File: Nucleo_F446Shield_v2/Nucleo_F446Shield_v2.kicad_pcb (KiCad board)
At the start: 2 copper layers, 48 parts, among them J1 Barrel_Jack, J11 CAN1, J12 CAN2, J15 CAN1, J16 CAN2, J19 I2C3, J20 UART4, J21 xt60 male, J3 CAN1, J4 CAN2, J7 CAN1, J8 CAN2, M3 TJA1050_Module, M4 TJA1050_Module, SW1 SW1, SW11 DIP1, SW2 SW2, SW3 SW3, U1 NUCLEO-F446RE, U2 MP1584

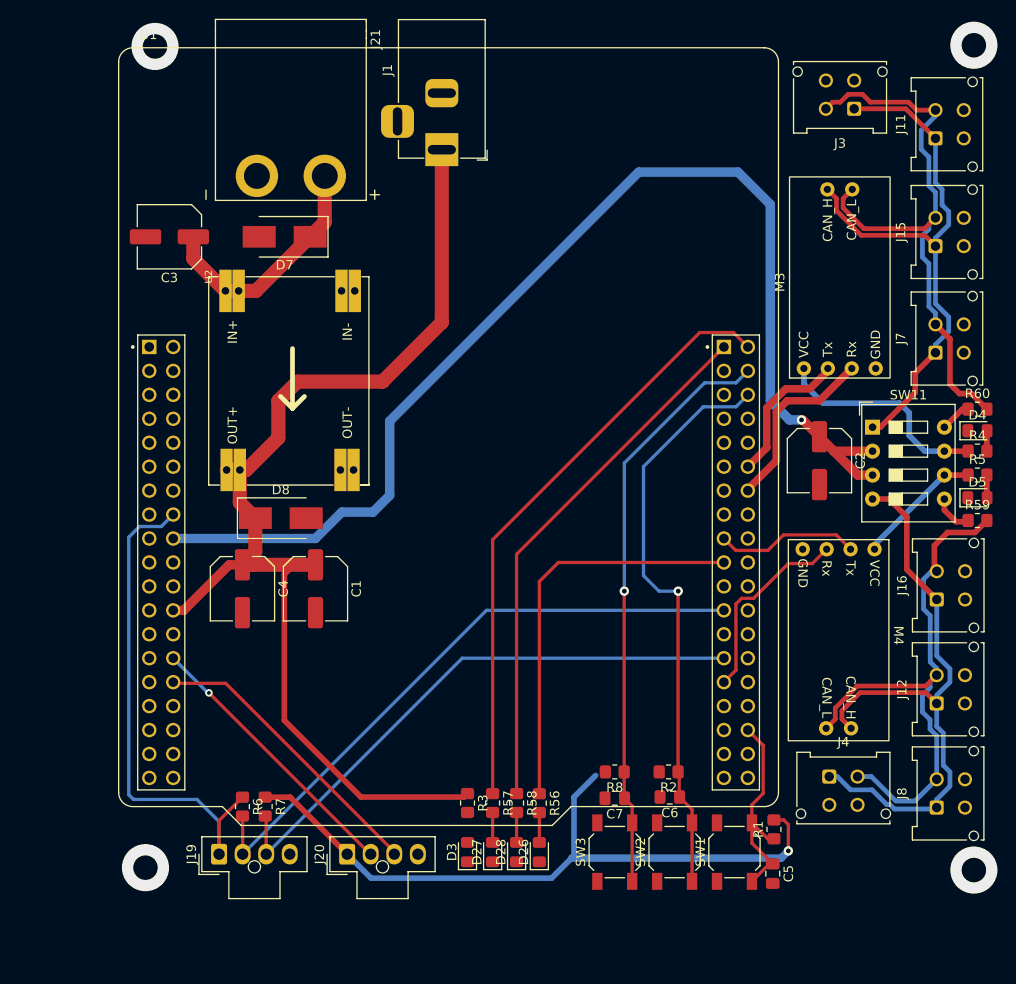
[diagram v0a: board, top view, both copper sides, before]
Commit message: add V2 board
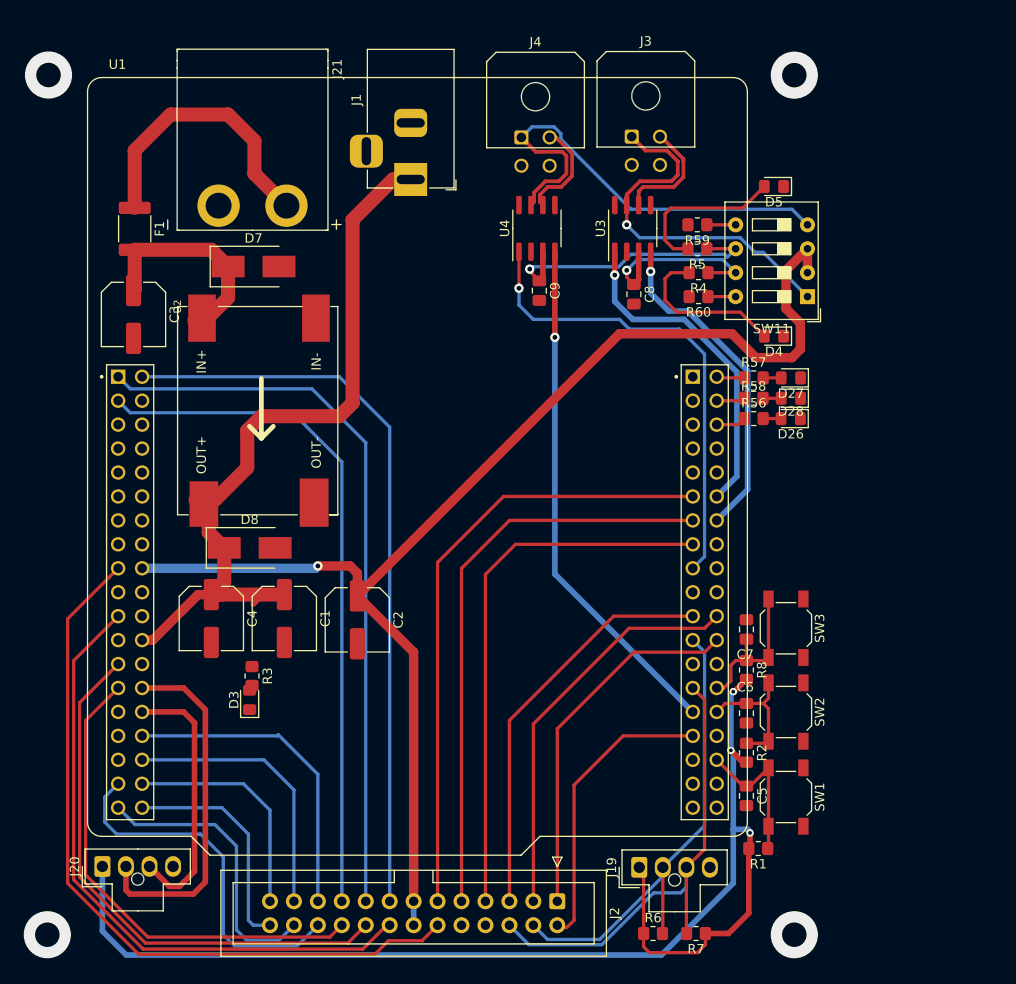
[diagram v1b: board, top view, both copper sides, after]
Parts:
- removed J11, J15, J7: CAN1, Connector_Molex:Molex_Micro-Fit_3.0_43045-0412_2x02_P3.00mm_Vertical
- removed J12, J16, J8: CAN2, Connector_Molex:Molex_Micro-Fit_3.0_43045-0412_2x02_P3.00mm_Vertical
- removed M3, M4: TJA1050_Module, PolyuRobotics:TJA1050_CAN_Module
- added C8: 100nF, Capacitor_SMD:C_0805_2012Metric_Pad1.18x1.45mm_HandSolder, F.Cu at (109.5, 60.2)
- added C9: 100nF, Capacitor_SMD:C_0805_2012Metric_Pad1.18x1.45mm_HandSolder, F.Cu at (99.4, 59.8)
- added F1: 24V 3A, Fuse:Fuse_1812_4532Metric_Pad1.30x3.40mm_HandSolder, F.Cu at (56.5, 53.3)
- added J2: Conn_02x13_Odd_Even, Connector_IDC:IDC-Header_2x13_P2.54mm_Vertical, F.Cu at (101.3, 124.6)
- added U3: TJA1050, Package_SO:SOIC-8_3.9x4.9mm_P1.27mm, F.Cu at (109.3, 53.2)
- added U4: TJA1050, Package_SO:SOIC-8_3.9x4.9mm_P1.27mm, F.Cu at (99.2, 53.2)
- D5: value can_led -> can2_led
- J3, J4: footprint Connector_Molex:Molex_Micro-Fit_3.0_43045-0412_2x02_P3.00mm_Vertical -> Connector_Molex:Molex_Micro-Fit_3.0_43045-0400_2x02_P3.00mm_Horizontal
- moved J4 75.3 mm to (97.5, 43.6)
- moved D27 59.4 mm to (126.1, 69.1), turned to 180 degrees
- moved D28 56.3 mm to (126.1, 71.2), turned to 180 degrees
- moved D26 53.2 mm to (126.1, 73.4), turned to 180 degrees
- moved R57 52.9 mm to (122.2, 69.1), turned to 0 degrees
- moved C2 51.9 mm to (80.1, 94.7)
- moved R58 49.8 mm to (122.2, 71.2), turned to 0 degrees
- moved R7 47.6 mm to (116.1, 128.0), turned to 180 degrees
- moved R56 46.7 mm to (122.2, 73.4), turned to 0 degrees
- moved R6 45.6 mm to (111.5, 128.0), turned to 0 degrees
- moved J19 44.6 mm to (110.0, 121.0)
- moved R59 43.2 mm to (116.2, 52.8), turned to 180 degrees
- moved D5 39.5 mm to (124.3, 48.8), turned to 180 degrees
- moved R5 38.2 mm to (116.2, 55.4), turned to 180 degrees
- moved R4 35.1 mm to (116.3, 57.9), turned to 180 degrees
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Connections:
- C3 pad 1: +24V -> Net-(C3-Pad1)
- C6 pad 1: /PC5 -> /PB13
- C7 pad 1: /PC6 -> /PB14
- D7 pad 1: +24V -> Net-(C3-Pad1)
- J3 pad 3: GND -> unconnected-(J3-Pad3)
- J4 pad 3: GND -> unconnected-(J4-Pad3)
- R2 pad 1: /PC5 -> /PB13
- R56 pad 1: /PC7 -> /PC5
- R58 pad 1: /PC9 -> /PC6
- R8 pad 1: /PC6 -> /PB14
- SW2 pad 2: /PC5 -> /PB13
- SW3 pad 2: /PC6 -> /PB14
- U1 pad CN10_11: unconnected-(U1-PadCN10_11) -> PA5
- U1 pad CN10_13: unconnected-(U1-PadCN10_13) -> PA6
- U1 pad CN10_15: unconnected-(U1-PadCN10_15) -> PA7
- U1 pad CN10_21: unconnected-(U1-PadCN10_21) -> PA9
- U1 pad CN10_22: unconnected-(U1-PadCN10_22) -> PB2
- U1 pad CN10_24: unconnected-(U1-PadCN10_24) -> PB1
- U1 pad CN10_28: unconnected-(U1-PadCN10_28) -> /PB14
- U1 pad CN10_30: unconnected-(U1-PadCN10_30) -> /PB13
- U1 pad CN10_31: unconnected-(U1-PadCN10_31) -> PB3
- U1 pad CN10_33: unconnected-(U1-PadCN10_33) -> /PA10
- U1 pad CN7_1: unconnected-(U1-PadCN7_1) -> PC10
- U1 pad CN7_17: unconnected-(U1-PadCN7_17) -> PA15
- U1 pad CN7_2: unconnected-(U1-PadCN7_2) -> PC11
- U1 pad CN7_21: unconnected-(U1-PadCN7_21) -> PB7
- U1 pad CN7_25: unconnected-(U1-PadCN7_25) -> PC14
- U1 pad CN7_27: unconnected-(U1-PadCN7_27) -> PC15
- U1 pad CN7_3: unconnected-(U1-PadCN7_3) -> PC12
- U1 pad CN7_32: unconnected-(U1-PadCN7_32) -> PA4
- U1 pad CN7_34: unconnected-(U1-PadCN7_34) -> PB0
- U1 pad CN7_35: unconnected-(U1-PadCN7_35) -> PC2
- U1 pad CN7_36: unconnected-(U1-PadCN7_36) -> PC1
- U1 pad CN7_37: unconnected-(U1-PadCN7_37) -> PC3
- U1 pad CN7_38: unconnected-(U1-PadCN7_38) -> PC0
- U2 pad IN1+: +24V -> Net-(C3-Pad1)
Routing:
- net PA15: track 0.00 -> 79.3 mm
- net PC11: track 0.00 -> 78.8 mm
- net PC10: track 0.00 -> 77.8 mm
- net PC12: track 0.00 -> 73.0 mm
- net PB7: track 0.00 -> 67.5 mm
- net PA5: track 0.00 -> 65.9 mm
- net PA6: track 0.00 -> 62.0 mm
- net /PC8: track 63.7 -> 2.98 mm
- net /PC6: track 61.9 -> 3.02 mm, vias 1 -> 0
- net PC14: track 0.00 -> 58.3 mm
- net /PC5: track 61.5 -> 3.20 mm, vias 1 -> 0
- net PA7: track 0.00 -> 58.0 mm
- net /PC9: track 56.5 -> 0.00 mm
- net PC15: track 0.00 -> 51.7 mm
- net /CAN1-: track 63.6 -> 12.5 mm
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
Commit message: add V2 board
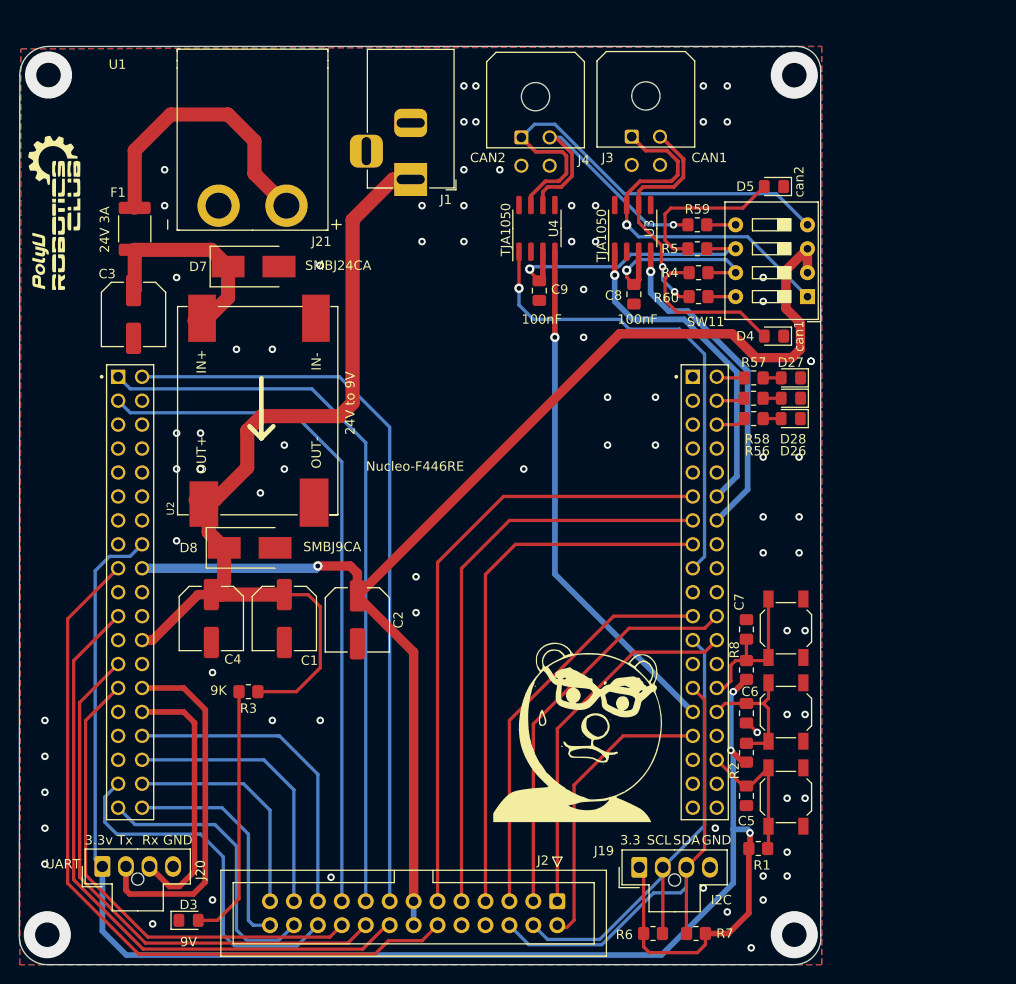
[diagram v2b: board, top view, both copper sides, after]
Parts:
- added G***: LOGO, PolyuRobotics:Raymond, F.Cu at (104.5, 106.2)
- added G***: LOGO, PolyuRobotics:Club_logo, F.Cu at (48.3, 51.4)
- added G***: LOGO, PolyuRobotics:BullyU_logo, B.Cu at (86.4, 88.3)
- moved D3 24.3 mm to (62.2, 126.6), turned to 0 degrees
- moved R3 1.71 mm to (68.6, 102.4), turned to 180 degrees
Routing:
- net +3V3: track 135.7 -> 173.5 mm
- net Net-(D3-Pad2): track 0.00 -> 27.2 mm
- net /CAN2-: track 11.2 -> 29.5 mm, vias 0 -> 1
- net VCC: track 83.7 -> 98.5 mm
- net /CAN1-: track 12.5 -> 25.5 mm, vias 0 -> 2
- net GND: track 0.09 -> 1.64 mm, vias 0 -> 79
- added copper zone on B.Cu, net GND
- added copper zone on F.Cu, net GND
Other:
- board outline added: 85 x 97.4 mm
- board text added: "100nF"
- board text added: "24V 3A"
- board text added: "24V IN"
- board text added: "24V to 9V"
- board text added: "3.3"
- board text added: "3.3v"
- board text added: "9K"
- board text added: "9V"
- board text added: "9V IN"
- board text added: "CAN 1"
- board text added: "CAN1"
- board text added: "CAN2"
- board text added: "GND"
- board text added: "I2C"
- board text added: "PB13"
- board text added: "PB14"
- board text added: "PC4"
- board text added: "PC8 PC6 PC5"
- board text added: "Rx"
- board text added: "SCL"
- board text added: "SDA"
- board text added: "SMBJ24CA"
- board text added: "SMBJ9CA"
- board text added: "TJA1050"
- board text added: "Tx"
- board text added: "UART"
- board text added: "can1"
- board text added: "can2"

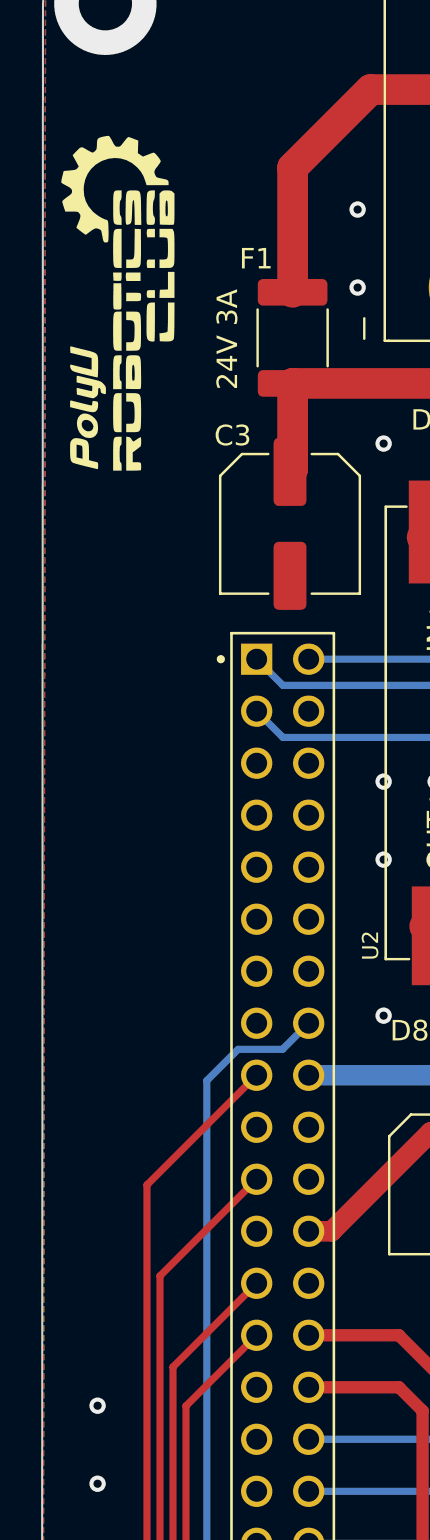
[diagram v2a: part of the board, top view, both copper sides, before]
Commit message: add V2 board
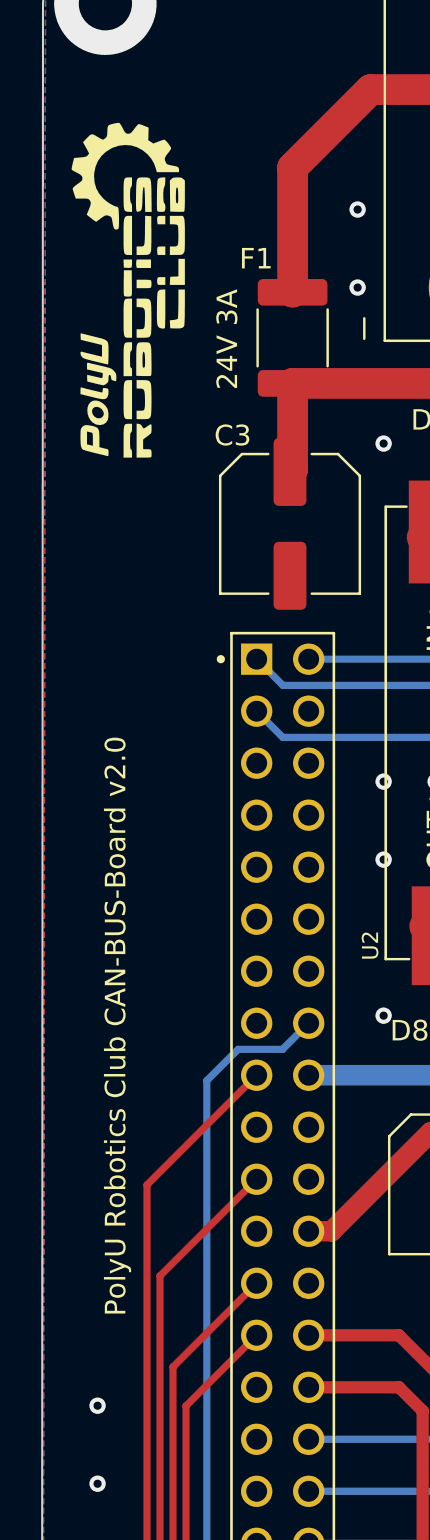
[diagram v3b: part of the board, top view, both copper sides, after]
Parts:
- moved G*** 0.81 mm to (48.8, 50.8)
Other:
- board text added: "5V"
- board text added: "PA15"
- board text added: "PA4"
- board text added: "PA5"
- board text added: "PA6"
- board text added: "PA7"
- board text added: "PA9"
- board text added: "PB0"
- board text added: "PB1"
- board text added: "PB2"
- board text added: "PB3"
- board text added: "PB7"
- board text added: "PC0"
- board text added: "PC1"
- board text added: "PC10"
- board text added: "PC11"
- board text added: "PC12"
- board text added: "PC14"
- board text added: "PC15"
- board text added: "PC2"
- board text added: "PC3"
- board text added: "PolyU Robotics Club CAN-BUS-Board v2.0"
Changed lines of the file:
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@@
   )
   (footprint "PolyuRobotics:Club_logo" (layer "F.Cu")
-    (at 48.26 51.435 90)
+    (at 48.768 50.8 90)
     (attr smd board_only exclude_from_pos_files exclude_from_bom)
     (fp_text reference "G***" (at 0 5.334 90) (layer "F.SilkS") hide
@@
   (gr_line (start 129.286 128.143) (end 129.286 36.449) (layer "Edge.Cuts") (width 0.1))
   (gr_arc (start 44.323 36.957) (mid 45.215739 34.801739) (end 47.371 33.909) (layer "Edge.Cuts") (width 0.1))
+  (gr_text "SCL" (at 98.806 129.667 270) (layer "B.SilkS")
+    (effects (font (size 1 1) (thickness 0.15)) (justify mirror))
+  )
+  (gr_text "PA15" (at 88.646 129.413 270) (layer "B.SilkS")
+    (effects (font (size 1 1) (thickness 0.15)) (justify mirror))
+  )
+  (gr_text "PC14" (at 81.026 129.413 270) (layer "B.SilkS")
+    (effects (font (size 1 1) (thickness 0.15)) (justify mirror))
+  )
   (gr_text "PB14" (at 124.46 95.885 90) (layer "B.SilkS")
     (effects (font (size 1 1) (thickness 0.15)) (justify mirror))
   )
+  (gr_text "PC11" (at 83.566 121.285 270) (layer "B.SilkS")
+    (effects (font (size 1 1) (thickness 0.15)) (justify mirror))
+  )
+  (gr_text "PA6" (at 91.186 121.666 270) (layer "B.SilkS")
+    (effects (font (size 1 1) (thickness 0.15)) (justify mirror))
+  )
+  (gr_text "PC3" (at 73.406 129.794 270) (layer "B.SilkS")
+    (effects (font (size 1 1) (thickness 0.15)) (justify mirror))
+  )
+  (gr_text "PC15" (at 78.486 129.413 270) (layer "B.SilkS")
+    (effects (font (size 1 1) (thickness 0.15)) (justify mirror))
+  )
+  (gr_text "PC10" (at 81.026 121.285 270) (layer "B.SilkS")
+    (effects (font (size 1 1) (thickness 0.15)) (justify mirror))
+  )
+  (gr_text "SDA" (at 96.266 129.667 270) (layer "B.SilkS")
+    (effects (font (size 1 1) (thickness 0.15)) (justify mirror))
+  )
+  (gr_text "PC12" (at 78.486 121.285 270) (layer "B.SilkS")
+    (effects (font (size 1 1) (thickness 0.15)) (justify mirror))
+  )
   (gr_text "PC4\n" (at 125.095 113.665 90) (layer "B.SilkS")
     (effects (font (size 1 1) (thickness 0.15)) (justify mirror))
   )
+  (gr_text "PA4" (at 75.819 121.793 270) (layer "B.SilkS")
+    (effects (font (size 1 1) (thickness 0.15)) (justify mirror))
+  )
+  (gr_text "PA9" (at 96.266 121.666 270) (layer "B.SilkS")
+    (effects (font (size 1 1) (thickness 0.15)) (justify mirror))
+  )
+  (gr_text "PB7" (at 83.566 129.794 270) (layer "B.SilkS")
+    (effects (font (size 1 1) (thickness 0.15)) (justify mirror))
+  )
+  (gr_text "PA7" (at 93.726 121.666 270) (layer "B.SilkS")
+    (effects (font (size 1 1) (thickness 0.15)) (justify mirror))
+  )
+  (gr_text "5V" (at 86.106 129.286 270) (layer "B.SilkS")
+    (effects (font (size 1 1) (thickness 0.15)) (justify mirror))
+  )
   (gr_text "CAN 1" (at 118.11 46.355) (layer "B.SilkS")
     (effects (font (size 1 1) (thickness 0.15)) (justify mirror))
   )
+  (gr_text "PA5" (at 88.646 121.666 270) (layer "B.SilkS")
+    (effects (font (size 1 1) (thickness 0.15)) (justify mirror))
+  )
+  (gr_text "PC2" (at 75.946 129.794 270) (layer "B.SilkS")
+    (effects (font (size 1 1) (thickness 0.15)) (justify mirror))
+  )
+  (gr_text "PC1" (at 70.866 121.666 270) (layer "B.SilkS")
+    (effects (font (size 1 1) (thickness 0.15)) (justify mirror))
+  )
+  (gr_text "PB1" (at 101.219 121.666 270) (layer "B.SilkS")
+    (effects (font (size 1 1) (thickness 0.15)) (justify mirror))
+  )
+  (gr_text "5V" (at 85.979 122.174 270) (layer "B.SilkS")
+    (effects (font (size 1 1) (thickness 0.15)) (justify mirror))
+  )
   (gr_text "PC8\nPC6\nPC5" (at 126.365 71.12) (layer "B.SilkS")
     (effects (font (size 1 1) (thickness 0.15)) (justify mirror))
   )
+  (gr_text "PC0" (at 70.739 129.794 270) (layer "B.SilkS")
+    (effects (font (size 1 1) (thickness 0.15)) (justify mirror))
+  )
   (gr_text "24V IN" (at 69.215 38.735) (layer "B.SilkS")
     (effects (font (size 1 1) (thickness 0.15)) (justify mirror))
@@
     (effects (font (size 1 1) (thickness 0.15)) (justify mirror))
   )
+  (gr_text "PB3" (at 101.346 129.667 270) (layer "B.SilkS")
+    (effects (font (size 1 1) (thickness 0.15)) (justify mirror))
+  )
+  (gr_text "PB0" (at 73.406 121.666 270) (layer "B.SilkS")
+    (effects (font (size 1 1) (thickness 0.15)) (justify mirror))
+  )
+  (gr_text "PB2" (at 98.806 121.666 270) (layer "B.SilkS")
+    (effects (font (size 1 1) (thickness 0.15)) (justify mirror))
+  )
   (gr_text "PB13\n" (at 124.46 104.775 90) (layer "B.SilkS")
     (effects (font (size 1 1) (thickness 0.15)) (justify mirror))
@@
     (effects (font (size 1 1) (thickness 0.15)))
   )
+  (gr_text "PolyU Robotics Club CAN-BUS-Board v2.0" (at 47.879 86.868 90) (layer "F.SilkS")
+    (effects (font (size 1 1) (thickness 0.15)))
+  )
